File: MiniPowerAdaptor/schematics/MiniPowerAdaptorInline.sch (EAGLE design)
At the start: 8 parts, among them IC1 LM317MBSTT3

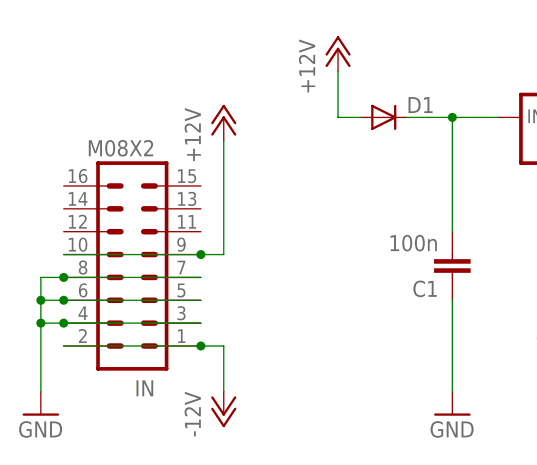
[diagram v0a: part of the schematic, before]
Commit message: inline 5v adaptor ordered from seeed
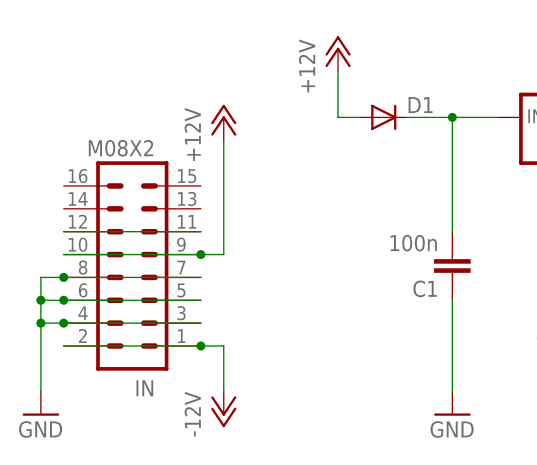
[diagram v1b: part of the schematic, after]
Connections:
- new net N$2: IN.11, IN.12
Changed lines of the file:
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@@
+</segment>
+</net>
+<net name="N$2" class="0">
+<segment>
+<pinref part="IN" gate="G$1" pin="12"/>
+<pinref part="IN" gate="G$1" pin="11"/>
+<wire x1="7.62" y1="38.1" x2="22.86" y2="38.1" width="0.1524" layer="91"/>
 </segment>
 </net>

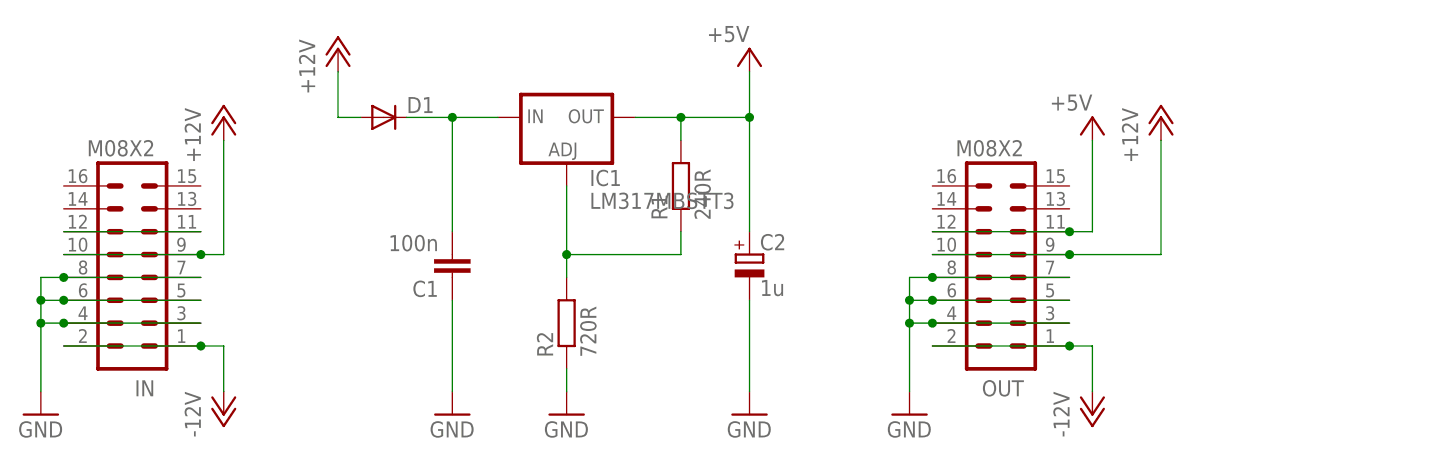
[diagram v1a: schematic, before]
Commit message: changed to dpak, changed electrolytic to 1206 cap and re-routed
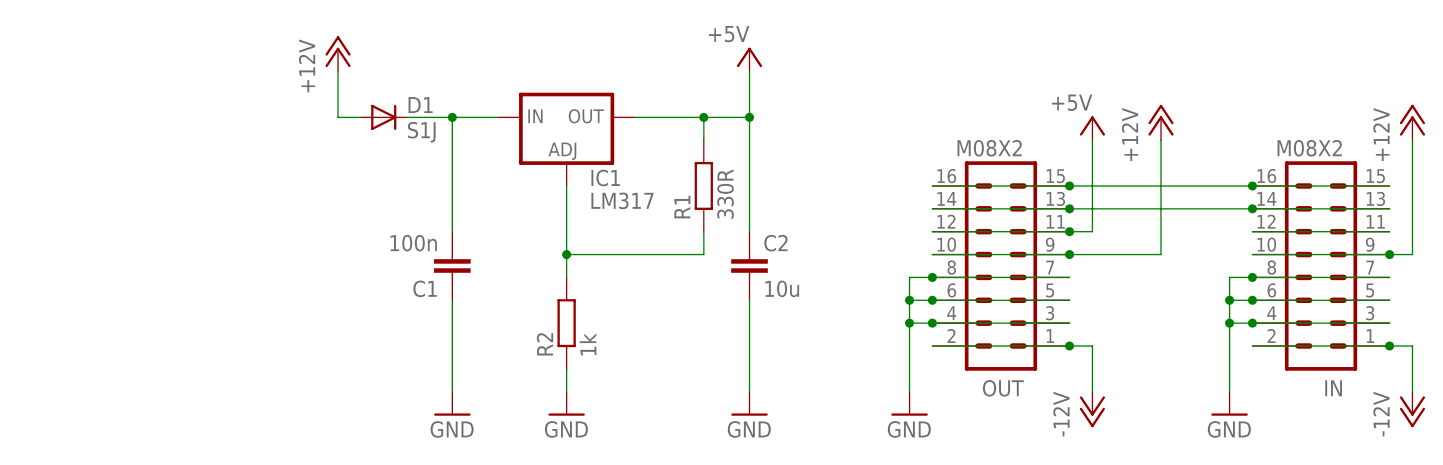
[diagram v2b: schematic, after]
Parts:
- C2: value 1u -> 10u; device rcl:CPOL-EUSANYO_SMD_A5 -> rcl:C-EUC1206
- D1: value (none) -> S1J
- IC1: value LM317MBSTT3 -> LM317; device v-reg:LM317MBSTT3 -> v-reg:LM317MDT
- R1: value 240R -> 330R
- R2: value 720R -> 1k
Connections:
- new net N$4: IN.13, IN.14, OUT.13, OUT.14
- new net N$5: IN.15, IN.16, OUT.15, OUT.16
- net +5V: now also C2.1; no longer C2.+
- net GND: now also C2.2; no longer C2.-
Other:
- moved on the sheet: IN, R1
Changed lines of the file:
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@@
 </classes>
 <parts>
-<part name="IC1" library="v-reg" deviceset="LM317?*" device="MBSTT3"/>
-<part name="R2" library="Rebel" deviceset="R-EU_" device="0603" value="720R"/>
-<part name="R1" library="Rebel" deviceset="R-EU_" device="0603" value="240R"/>
+<part name="IC1" library="v-reg" deviceset="LM317?*" device="" technology="MDT" value="LM317"/>
+<part name="R2" library="Rebel" deviceset="R-EU_" device="0603" value="1k"/>
+<part name="R1" library="Rebel" deviceset="R-EU_" device="0603" value="330R"/>
 <part name="C1" library="rcl" deviceset="C-EU" device="C0603" value="100n"/>
 <part name="P+12" library="supply1" deviceset="+5V" device=""/>
@@
 <part name="GND33" library="supply1" deviceset="GND" device=""/>
 <part name="P-2" library="supply1" deviceset="-12V" device=""/>
-<part name="C2" library="rcl" deviceset="CPOL-EU" device="SANYO_SMD_A5" value="1u"/>
+<part name="C2" library="rcl" deviceset="C-EU" device="C1206" value="10u"/>
 <part name="GND1" library="supply1" deviceset="GND" device=""/>
 <part name="GND4" library="supply1" deviceset="GND" device=""/>
 <part name="GND2" library="supply1" deviceset="GND" device=""/>
-<part name="D1" library="SparkFun" deviceset="DIODE" device="SMA"/>
+<part name="D1" library="SparkFun" deviceset="DIODE" device="SMA" value="S1J"/>
 <part name="P+1" library="supply1" deviceset="+12V" device=""/>
 <part name="P+2" library="supply1" deviceset="+5V" device=""/>
@@
 <instance part="IC1" gate="G$1" x="63.5" y="50.8"/>
 <instance part="R2" gate="G$1" x="63.5" y="27.94" rot="R90"/>
-<instance part="R1" gate="G$1" x="76.2" y="43.18" rot="R90"/>
+<instance part="R1" gate="G$1" x="78.74" y="43.18" rot="R90"/>
 <instance part="C1" gate="G$1" x="50.8" y="33.02" rot="R180"/>
 <instance part="P+12" gate="1" x="121.92" y="50.8" smashed="yes">
@@
 <attribute name="VALUE" x="83.82" y="60.96" size="1.778" layer="96" rot="R180"/>
 </instance>
-<instance part="IN" gate="G$1" x="15.24" y="35.56" rot="R180"/>
-<instance part="GND3" gate="1" x="5.08" y="17.78"/>
-<instance part="P-1" gate="1" x="25.4" y="17.78"/>
-<instance part="P+3" gate="1" x="25.4" y="50.8"/>
+<instance part="IN" gate="G$1" x="147.32" y="35.56" rot="R180"/>
+<instance part="GND3" gate="1" x="137.16" y="17.78"/>
+<instance part="P-1" gate="1" x="157.48" y="17.78"/>
+<instance part="P+3" gate="1" x="157.48" y="50.8"/>
 </instances>
 <busses>
@@
 <pinref part="IN" gate="G$1" pin="9"/>
 <pinref part="P+3" gate="1" pin="+12V"/>
-<wire x1="22.86" y1="35.56" x2="25.4" y2="35.56" width="0.1524" layer="91"/>
-<wire x1="25.4" y1="35.56" x2="25.4" y2="48.26" width="0.1524" layer="91"/>
+<wire x1="154.94" y1="35.56" x2="157.48" y2="35.56" width="0.1524" layer="91"/>
+<wire x1="157.48" y1="35.56" x2="157.48" y2="48.26" width="0.1524" layer="91"/>
 <pinref part="IN" gate="G$1" pin="10"/>
-<wire x1="7.62" y1="35.56" x2="22.86" y2="35.56" width="0.1524" layer="91"/>
-<junction x="22.86" y="35.56"/>
+<wire x1="139.7" y1="35.56" x2="154.94" y2="35.56" width="0.1524" layer="91"/>
+<junction x="154.94" y="35.56"/>
 </segment>
 <segment>
@@
 </segment>
 <segment>
-<pinref part="C2" gate="G$1" pin="-"/>
+<pinref part="C2" gate="G$1" pin="2"/>
 <pinref part="GND4" gate="1" pin="GND"/>
 <wire x1="83.82" y1="20.32" x2="83.82" y2="30.48" width="0.1524" layer="91"/>
@@
 <pinref part="IN" gate="G$1" pin="4"/>
 <pinref part="GND3" gate="1" pin="GND"/>
-<wire x1="7.62" y1="27.94" x2="5.08" y2="27.94" width="0.1524" layer="91"/>
-<wire x1="5.08" y1="27.94" x2="5.08" y2="20.32" width="0.1524" layer="91"/>
+<wire x1="139.7" y1="27.94" x2="137.16" y2="27.94" width="0.1524" layer="91"/>
+<wire x1="137.16" y1="27.94" x2="137.16" y2="20.32" width="0.1524" layer="91"/>
 <pinref part="IN" gate="G$1" pin="6"/>
-<wire x1="7.62" y1="30.48" x2="5.08" y2="30.48" width="0.1524" layer="91"/>
-<wire x1="5.08" y1="30.48" x2="5.08" y2="27.94" width="0.1524" layer="91"/>
-<junction x="5.08" y="27.94"/>
+<wire x1="139.7" y1="30.48" x2="137.16" y2="30.48" width="0.1524" layer="91"/>
+<wire x1="137.16" y1="30.48" x2="137.16" y2="27.94" width="0.1524" layer="91"/>
+<junction x="137.16" y="27.94"/>
 <pinref part="IN" gate="G$1" pin="8"/>
-<wire x1="7.62" y1="33.02" x2="5.08" y2="33.02" width="0.1524" layer="91"/>
-<wire x1="5.08" y1="33.02" x2="5.08" y2="30.48" width="0.1524" layer="91"/>
-<junction x="5.08" y="30.48"/>
+<wire x1="139.7" y1="33.02" x2="137.16" y2="33.02" width="0.1524" layer="91"/>
+<wire x1="137.16" y1="33.02" x2="137.16" y2="30.48" width="0.1524" layer="91"/>
+<junction x="137.16" y="30.48"/>
 <pinref part="IN" gate="G$1" pin="3"/>
-<wire x1="22.86" y1="27.94" x2="7.62" y2="27.94" width="0.1524" layer="91"/>
-<junction x="7.62" y="27.94"/>
+<wire x1="154.94" y1="27.94" x2="139.7" y2="27.94" width="0.1524" layer="91"/>
+<junction x="139.7" y="27.94"/>
 <pinref part="IN" gate="G$1" pin="5"/>
-<wire x1="7.62" y1="30.48" x2="22.86" y2="30.48" width="0.1524" layer="91"/>
-<junction x="7.62" y="30.48"/>
+<wire x1="139.7" y1="30.48" x2="154.94" y2="30.48" width="0.1524" layer="91"/>
+<junction x="139.7" y="30.48"/>
 <pinref part="IN" gate="G$1" pin="7"/>
-<wire x1="7.62" y1="33.02" x2="22.86" y2="33.02" width="0.1524" layer="91"/>
-<junction x="7.62" y="33.02"/>
+<wire x1="139.7" y1="33.02" x2="154.94" y2="33.02" width="0.1524" layer="91"/>
+<junction x="139.7" y="33.02"/>
 </segment>
 </net>
@@
 <pinref part="IN" gate="G$1" pin="1"/>
 <pinref part="P-1" gate="1" pin="-12V"/>
-<wire x1="22.86" y1="25.4" x2="25.4" y2="25.4" width="0.1524" layer="91"/>
-<wire x1="25.4" y1="25.4" x2="25.4" y2="20.32" width="0.1524" layer="91"/>
+<wire x1="154.94" y1="25.4" x2="157.48" y2="25.4" width="0.1524" layer="91"/>
+<wire x1="157.48" y1="25.4" x2="157.48" y2="20.32" width="0.1524" layer="91"/>
 <pinref part="IN" gate="G$1" pin="2"/>
-<wire x1="7.62" y1="25.4" x2="22.86" y2="25.4" width="0.1524" layer="91"/>
-<junction x="22.86" y="25.4"/>
+<wire x1="139.7" y1="25.4" x2="154.94" y2="25.4" width="0.1524" layer="91"/>
+<junction x="154.94" y="25.4"/>
 </segment>
 <segment>
@@
 <pinref part="IC1" gate="G$1" pin="OUT"/>
 <pinref part="R1" gate="G$1" pin="2"/>
-<wire x1="71.12" y1="50.8" x2="76.2" y2="50.8" width="0.1524" layer="91"/>
-<wire x1="76.2" y1="50.8" x2="76.2" y2="48.26" width="0.1524" layer="91"/>
-<pinref part="C2" gate="G$1" pin="+"/>
-<wire x1="76.2" y1="50.8" x2="83.82" y2="50.8" width="0.1524" layer="91"/>
+<wire x1="71.12" y1="50.8" x2="78.74" y2="50.8" width="0.1524" layer="91"/>
+<wire x1="78.74" y1="50.8" x2="78.74" y2="48.26" width="0.1524" layer="91"/>
+<pinref part="C2" gate="G$1" pin="1"/>
+<wire x1="78.74" y1="50.8" x2="83.82" y2="50.8" width="0.1524" layer="91"/>
 <wire x1="83.82" y1="50.8" x2="83.82" y2="38.1" width="0.1524" layer="91"/>
-<junction x="76.2" y="50.8"/>
+<junction x="78.74" y="50.8"/>
 <pinref part="P+2" gate="1" pin="+5V"/>
 <wire x1="83.82" y1="50.8" x2="83.82" y2="55.88" width="0.1524" layer="91"/>
@@
 <pinref part="R1" gate="G$1" pin="1"/>
 <wire x1="63.5" y1="35.56" x2="63.5" y2="43.18" width="0.1524" layer="91"/>
-<wire x1="76.2" y1="38.1" x2="76.2" y2="35.56" width="0.1524" layer="91"/>
-<wire x1="76.2" y1="35.56" x2="63.5" y2="35.56" width="0.1524" layer="91"/>
+<wire x1="78.74" y1="38.1" x2="78.74" y2="35.56" width="0.1524" layer="91"/>
+<wire x1="78.74" y1="35.56" x2="63.5" y2="35.56" width="0.1524" layer="91"/>
 <junction x="63.5" y="35.56"/>
 </segment>
@@
 <pinref part="IN" gate="G$1" pin="12"/>
 <pinref part="IN" gate="G$1" pin="11"/>
-<wire x1="7.62" y1="38.1" x2="22.86" y2="38.1" width="0.1524" layer="91"/>
-</segment>
-</net>
+<wire x1="139.7" y1="38.1" x2="154.94" y2="38.1" width="0.1524" layer="91"/>
+</segment>
+</net>
+<net name="N$4" class="0">
+<segment>
+<pinref part="OUT" gate="G$1" pin="14"/>
+<pinref part="OUT" gate="G$1" pin="13"/>
+<wire x1="104.14" y1="40.64" x2="119.38" y2="40.64" width="0.1524" layer="91"/>
+<pinref part="IN" gate="G$1" pin="14"/>
+<wire x1="119.38" y1="40.64" x2="139.7" y2="40.64" width="0.1524" layer="91"/>
+<junction x="119.38" y="40.64"/>
+<pinref part="IN" gate="G$1" pin="13"/>
+<wire x1="154.94" y1="40.64" x2="139.7" y2="40.64" width="0.1524" layer="91"/>
+<junction x="139.7" y="40.64"/>
+</segment>
+</net>
+<net name="N$5" class="0">
+<segment>
+<pinref part="IN" gate="G$1" pin="15"/>
+<pinref part="IN" gate="G$1" pin="16"/>
+<wire x1="154.94" y1="43.18" x2="139.7" y2="43.18" width="0.1524" layer="91"/>
+<pinref part="OUT" gate="G$1" pin="15"/>
+<wire x1="139.7" y1="43.18" x2="119.38" y2="43.18" width="0.1524" layer="91"/>
+<junction x="139.7" y="43.18"/>
+<pinref part="OUT" gate="G$1" pin="16"/>
+<wire x1="119.38" y1="43.18" x2="104.14" y2="43.18" width="0.1524" layer="91"/>
+<junction x="119.38" y="43.18"/>
+</segment>
+</net>

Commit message: Rev03
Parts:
- removed IN: M08X2, SparkFun:M08X2
- added JP1: (no value), pinhead:PINHD-2X5
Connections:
- removed net N$2: IN.11, IN.12
- removed net N$4: IN.13, IN.14, OUT.13, OUT.14
- removed net N$5: IN.15, IN.16, OUT.15, OUT.16
- net +12V: now also JP1.10, JP1.9; no longer IN.10, IN.9
- net -12V: now also JP1.1, JP1.2; no longer IN.1, IN.2
- net GND: now also JP1.3, JP1.4, JP1.5, JP1.6, JP1.7, JP1.8; no longer IN.3, IN.4, IN.5, IN.6, IN.7, IN.8
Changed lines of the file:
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@@
 <?xml version="1.0" encoding="utf-8"?>
 <!DOCTYPE eagle SYSTEM "eagle.dtd">
-<eagle version="6.6.0">
+<eagle version="7.5.0">
 <drawing>
 <settings>
@@
 <part name="P+1" library="supply1" deviceset="+12V" device=""/>
 <part name="P+2" library="supply1" deviceset="+5V" device=""/>
-<part name="IN" library="SparkFun" deviceset="M08X2" device=""/>
 <part name="GND3" library="supply1" deviceset="GND" device=""/>
 <part name="P-1" library="supply1" deviceset="-12V" device=""/>
 <part name="P+3" library="supply1" deviceset="+12V" device=""/>
+<part name="JP1" library="pinhead" deviceset="PINHD-2X5" device=""/>
 </parts>
 <sheets>
@@
 <attribute name="VALUE" x="83.82" y="60.96" size="1.778" layer="96" rot="R180"/>
 </instance>
-<instance part="IN" gate="G$1" x="147.32" y="35.56" rot="R180"/>
 <instance part="GND3" gate="1" x="137.16" y="17.78"/>
 <instance part="P-1" gate="1" x="157.48" y="17.78"/>
 <instance part="P+3" gate="1" x="157.48" y="50.8"/>
+<instance part="JP1" gate="A" x="149.86" y="30.48" rot="R180"/>
 </instances>
 <busses>
@@
 </segment>
 <segment>
-<pinref part="IN" gate="G$1" pin="9"/>
 <pinref part="P+3" gate="1" pin="+12V"/>
 <wire x1="154.94" y1="35.56" x2="157.48" y2="35.56" width="0.1524" layer="91"/>
 <wire x1="157.48" y1="35.56" x2="157.48" y2="48.26" width="0.1524" layer="91"/>
-<pinref part="IN" gate="G$1" pin="10"/>
-<wire x1="139.7" y1="35.56" x2="154.94" y2="35.56" width="0.1524" layer="91"/>
-<junction x="154.94" y="35.56"/>
+<wire x1="139.7" y1="35.56" x2="144.78" y2="35.56" width="0.1524" layer="91"/>
+<pinref part="JP1" gate="A" pin="9"/>
+<wire x1="144.78" y1="35.56" x2="152.4" y2="35.56" width="0.1524" layer="91"/>
+<wire x1="152.4" y1="35.56" x2="154.94" y2="35.56" width="0.1524" layer="91"/>
+<junction x="152.4" y="35.56"/>
+<pinref part="JP1" gate="A" pin="10"/>
+<junction x="144.78" y="35.56"/>
 </segment>
 <segment>
@@
 </segment>
 <segment>
-<pinref part="IN" gate="G$1" pin="4"/>
 <pinref part="GND3" gate="1" pin="GND"/>
 <wire x1="139.7" y1="27.94" x2="137.16" y2="27.94" width="0.1524" layer="91"/>
 <wire x1="137.16" y1="27.94" x2="137.16" y2="20.32" width="0.1524" layer="91"/>
-<pinref part="IN" gate="G$1" pin="6"/>
 <wire x1="139.7" y1="30.48" x2="137.16" y2="30.48" width="0.1524" layer="91"/>
 <wire x1="137.16" y1="30.48" x2="137.16" y2="27.94" width="0.1524" layer="91"/>
 <junction x="137.16" y="27.94"/>
-<pinref part="IN" gate="G$1" pin="8"/>
 <wire x1="139.7" y1="33.02" x2="137.16" y2="33.02" width="0.1524" layer="91"/>
 <wire x1="137.16" y1="33.02" x2="137.16" y2="30.48" width="0.1524" layer="91"/>
 <junction x="137.16" y="30.48"/>
-<pinref part="IN" gate="G$1" pin="3"/>
-<wire x1="154.94" y1="27.94" x2="139.7" y2="27.94" width="0.1524" layer="91"/>
-<junction x="139.7" y="27.94"/>
-<pinref part="IN" gate="G$1" pin="5"/>
-<wire x1="139.7" y1="30.48" x2="154.94" y2="30.48" width="0.1524" layer="91"/>
-<junction x="139.7" y="30.48"/>
-<pinref part="IN" gate="G$1" pin="7"/>
-<wire x1="139.7" y1="33.02" x2="154.94" y2="33.02" width="0.1524" layer="91"/>
-<junction x="139.7" y="33.02"/>
+<wire x1="154.94" y1="27.94" x2="152.4" y2="27.94" width="0.1524" layer="91"/>
+<wire x1="152.4" y1="27.94" x2="144.78" y2="27.94" width="0.1524" layer="91"/>
+<wire x1="144.78" y1="27.94" x2="139.7" y2="27.94" width="0.1524" layer="91"/>
+<wire x1="139.7" y1="30.48" x2="144.78" y2="30.48" width="0.1524" layer="91"/>
+<wire x1="144.78" y1="30.48" x2="152.4" y2="30.48" width="0.1524" layer="91"/>
+<wire x1="152.4" y1="30.48" x2="154.94" y2="30.48" width="0.1524" layer="91"/>
+<wire x1="139.7" y1="33.02" x2="144.78" y2="33.02" width="0.1524" layer="91"/>
+<pinref part="JP1" gate="A" pin="3"/>
+<junction x="152.4" y="27.94"/>
+<pinref part="JP1" gate="A" pin="4"/>
+<junction x="144.78" y="27.94"/>
+<pinref part="JP1" gate="A" pin="5"/>
+<junction x="152.4" y="30.48"/>
+<pinref part="JP1" gate="A" pin="6"/>
+<junction x="144.78" y="30.48"/>
+<pinref part="JP1" gate="A" pin="7"/>
+<wire x1="144.78" y1="33.02" x2="152.4" y2="33.02" width="0.1524" layer="91"/>
+<wire x1="152.4" y1="33.02" x2="154.94" y2="33.02" width="0.1524" layer="91"/>
+<junction x="152.4" y="33.02"/>
+<pinref part="JP1" gate="A" pin="8"/>
+<junction x="144.78" y="33.02"/>
 </segment>
 </net>
 <net name="-12V" class="0">
 <segment>
-<pinref part="IN" gate="G$1" pin="1"/>
 <pinref part="P-1" gate="1" pin="-12V"/>
 <wire x1="154.94" y1="25.4" x2="157.48" y2="25.4" width="0.1524" layer="91"/>
 <wire x1="157.48" y1="25.4" x2="157.48" y2="20.32" width="0.1524" layer="91"/>
-<pinref part="IN" gate="G$1" pin="2"/>
-<wire x1="139.7" y1="25.4" x2="154.94" y2="25.4" width="0.1524" layer="91"/>
-<junction x="154.94" y="25.4"/>
+<wire x1="139.7" y1="25.4" x2="144.78" y2="25.4" width="0.1524" layer="91"/>
+<pinref part="JP1" gate="A" pin="1"/>
+<wire x1="144.78" y1="25.4" x2="152.4" y2="25.4" width="0.1524" layer="91"/>
+<wire x1="152.4" y1="25.4" x2="154.94" y2="25.4" width="0.1524" layer="91"/>
+<junction x="152.4" y="25.4"/>
+<pinref part="JP1" gate="A" pin="2"/>
+<junction x="144.78" y="25.4"/>
 </segment>
 <segment>
@@
 </segment>
 </net>
-<net name="N$2" class="0">
-<segment>
-<pinref part="IN" gate="G$1" pin="12"/>
-<pinref part="IN" gate="G$1" pin="11"/>
-<wire x1="139.7" y1="38.1" x2="154.94" y2="38.1" width="0.1524" layer="91"/>
-</segment>
-</net>
-<net name="N$4" class="0">
-<segment>
-<pinref part="OUT" gate="G$1" pin="14"/>
-<pinref part="OUT" gate="G$1" pin="13"/>
-<wire x1="104.14" y1="40.64" x2="119.38" y2="40.64" width="0.1524" layer="91"/>
-<pinref part="IN" gate="G$1" pin="14"/>
-<wire x1="119.38" y1="40.64" x2="139.7" y2="40.64" width="0.1524" layer="91"/>
-<junction x="119.38" y="40.64"/>
-<pinref part="IN" gate="G$1" pin="13"/>
-<wire x1="154.94" y1="40.64" x2="139.7" y2="40.64" width="0.1524" layer="91"/>
-<junction x="139.7" y="40.64"/>
-</segment>
-</net>
-<net name="N$5" class="0">
-<segment>
-<pinref part="IN" gate="G$1" pin="15"/>
-<pinref part="IN" gate="G$1" pin="16"/>
-<wire x1="154.94" y1="43.18" x2="139.7" y2="43.18" width="0.1524" layer="91"/>
-<pinref part="OUT" gate="G$1" pin="15"/>
-<wire x1="139.7" y1="43.18" x2="119.38" y2="43.18" width="0.1524" layer="91"/>
-<junction x="139.7" y="43.18"/>
-<pinref part="OUT" gate="G$1" pin="16"/>
-<wire x1="119.38" y1="43.18" x2="104.14" y2="43.18" width="0.1524" layer="91"/>
-<junction x="119.38" y="43.18"/>
-</segment>
-</net>
